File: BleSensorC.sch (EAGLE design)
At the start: 14 parts, among them IC1 SI7020-A10-GM, U1 PIC18(L)F14K22-SOIC

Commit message: Fusion 3D support
Fusion 3D support
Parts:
- removed JP2: (no value), pinhead:PINHD-1X2/90
- removed U$3: SMTU2450N-LF, Battery holders:SMTU2450N-LF
- added B1: SMTU2450N-LF.TR, esao:SMTU2450N-LF.TR
- added C6: 1nF, resistor:C-EUC0805
- added C7: 1uF, resistor:C-EUC0805
- added MK1: SPH0644HM4H-1-3D, esao:SPH0644HM4H-1-3D
- added Q1: SI2333DDS-T1-GE3, esao:SI2333DDS-T1-GE3
- added R4: 4k7, resistor:R-EU_R0805
- added T1: BPW85C-L90, esao:BPW85C-L90
- C5: value 1nF -> 100nF
- IC1: value SI7020-A10-GM -> SI7020-A20-GM; device si70xx-10:SI7020-A10-GM -> esao:SI7020-A20-GM
- JP1: value (none) -> PINHD-1X8; device pinhead:PINHD-1X6 -> esao:PINHD-1X8
- R1, R2, R3: device resistor:R-EU_M0805 -> resistor:R-EU_R0805
- U1: value PIC18(L)F14K22-SOIC -> PIC16LF18446-I_SS; device Microchip PIC18F12K44_esao:PIC18(L)F14K22-SOIC -> SamacSys_Parts:PIC16LF18446-I_SS
- U2: value (none) -> RN4871-I; device Microchip RN4871:RN4871SMD -> esao:RN4871-I
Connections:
- removed net RA3_MCLR_VPP: JP1.1, U1.RA3/MCRL/VPP
- removed net SCL: IC1.SCL, R3.2, U1.RB6
- removed net SDA: IC1.SDA, R2.2, U1.RB4
- removed net U_MON: U1.RA2
- new net !MCLR!_VPP_RA3: JP1.1, U1.!MCLR!/VPP/RA3
- new net +B: B1.+B, Q1.D
- new net SCL1: IC1.SCL, R3.2, U1.RC0
- new net SCL2: MK1.CLOCK, U1.RC6
- new net SDA1: IC1.SDA, R2.2, U1.RC1
- new net SDA2: MK1.DATA, U1.RC7
- net GND: now also B1.-B, C6.2, C7.2, IC1.TGND, MK1.GND_1, MK1.GND_2, Q1.G, U2.GND13; no longer U$3.-B, U2.GND
- net IMP: now also C6.1, T1.E; no longer C5.1, JP2.2
- net PIC_RX: now also U1.RC5; no longer U1.RB5/RX/DT
- net PIC_TX: now also U1.RC4; no longer U1.RB7/TX/CK
- net RA0_ICSPDAT: now also U1.RA0/ICSPDAT; no longer U1.RA0
- net RA1_ICSPCLK: now also U1.RA1/ICSPCLK; no longer U1.RA1
- net RST: now also C7.1, R4.1, U2.RST; no longer U2.RST_N
- net UART_RX_IND: now also U1.RC3; no longer U1.RC0
- net VDD: now also C5.1, MK1.SELECT, MK1.VDD, Q1.S, R4.2, T1.C; no longer JP2.1, U$3.+B
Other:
- note added: "IC1"
- note added: "MK1"
- note removed: "C1"
- moved on the sheet: C3, C4, C5, R1, R2, R3

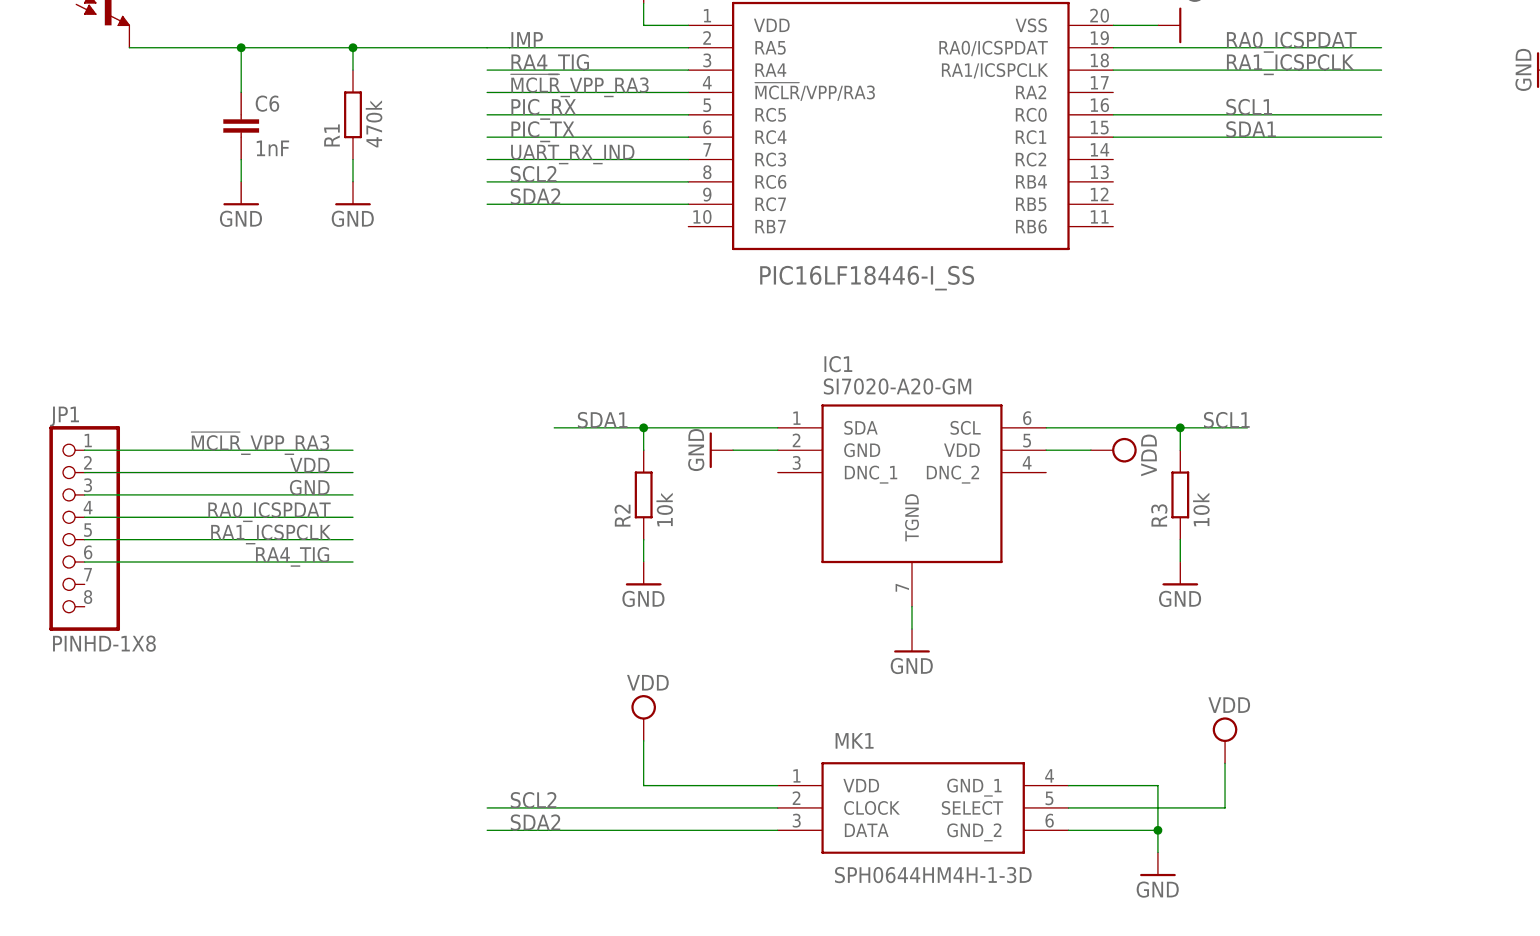
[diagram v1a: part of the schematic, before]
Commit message: JP1 & JP2
JP1 1X6
JP2 2X3
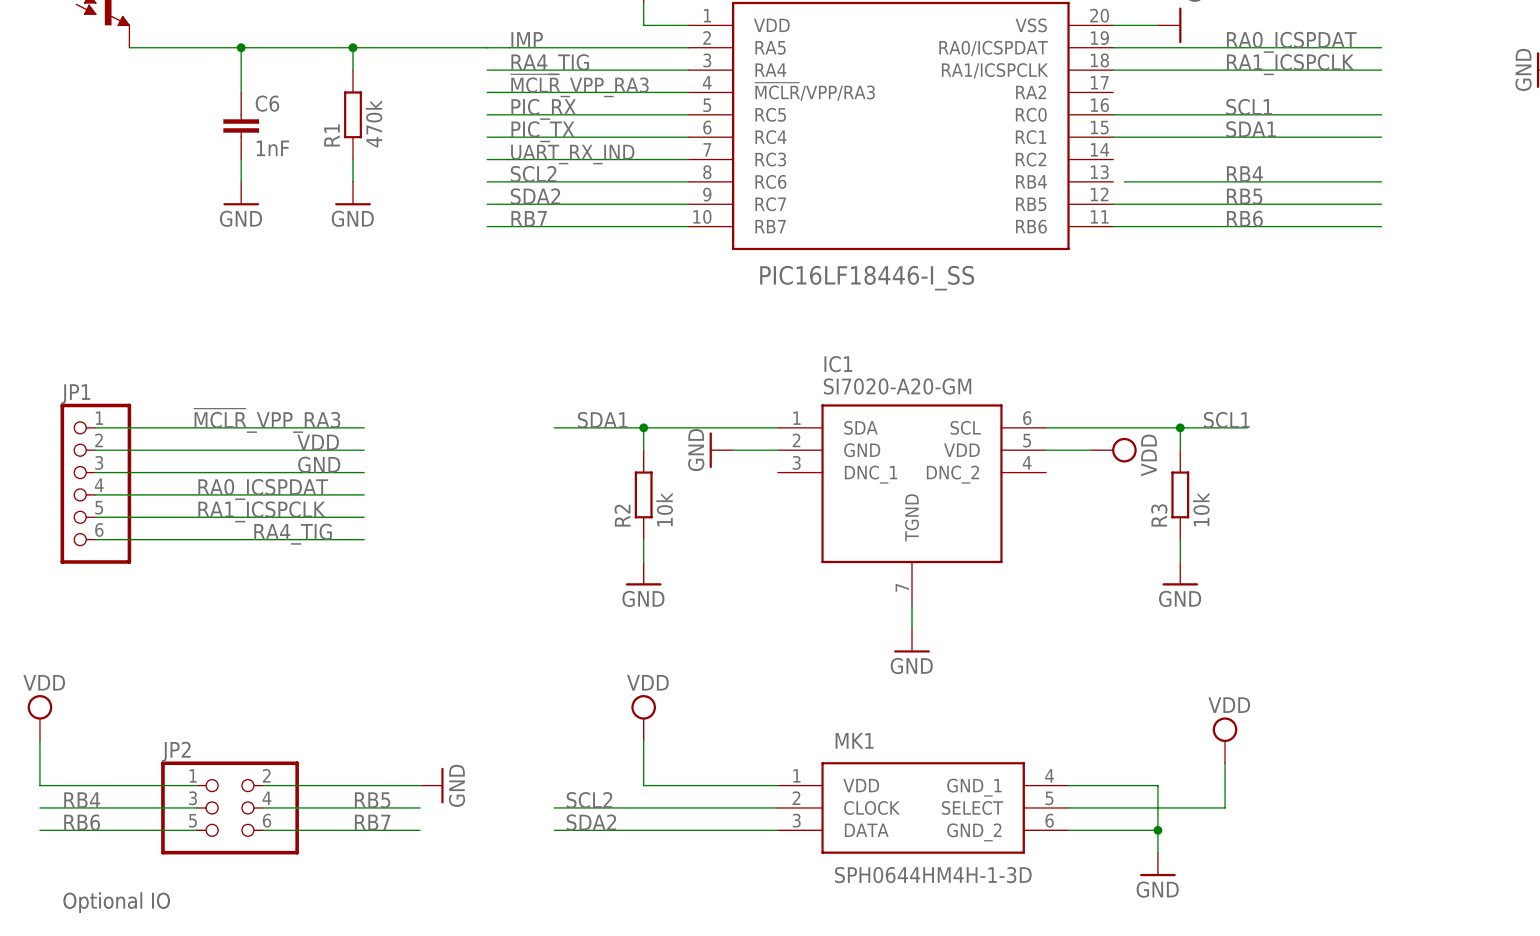
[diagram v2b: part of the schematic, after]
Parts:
- added JP2: (no value), pinhead:PINHD-2X3
- JP1: value PINHD-1X8 -> (none); device esao:PINHD-1X8 -> esao:PINHD-1X6-S
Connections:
- new net RB4: JP2.3
- new net RB5: JP2.4, U1.RB5
- new net RB6: JP2.5, U1.RB6
- new net RB7: JP2.6, U1.RB7
- net GND: now also JP2.2
- net VDD: now also JP2.1
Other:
- note added: "Optional IO"

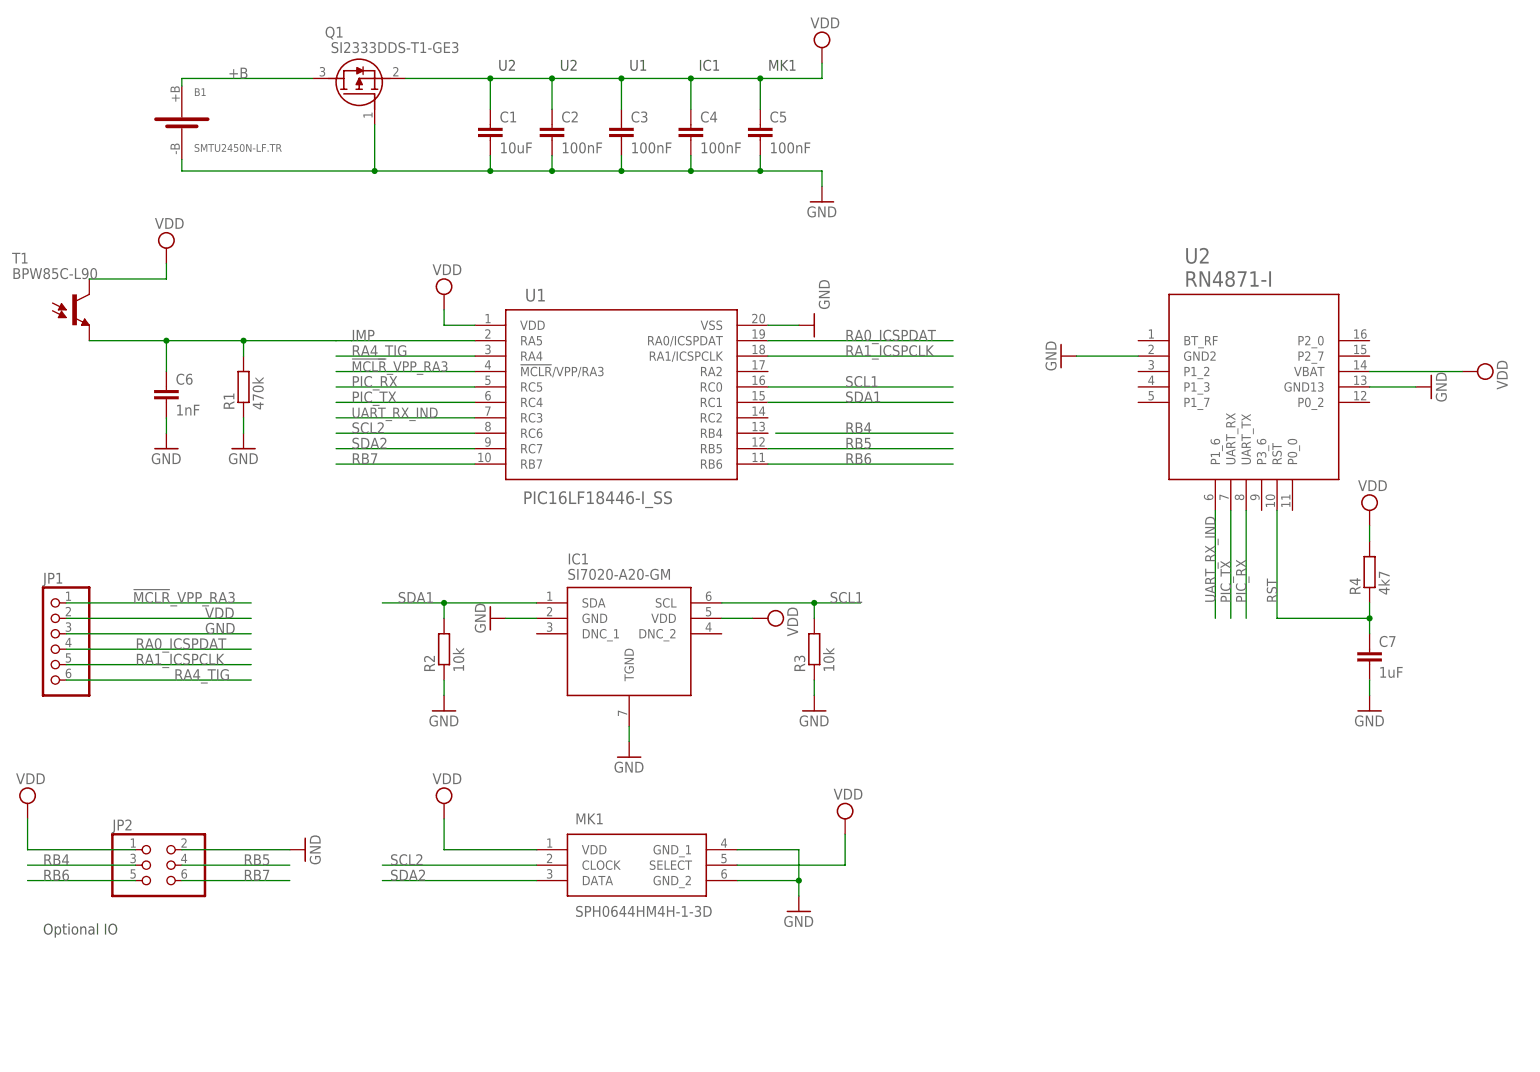
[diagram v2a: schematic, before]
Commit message: T1 phototransistor
Changed T1 to Vishay VEMT2523
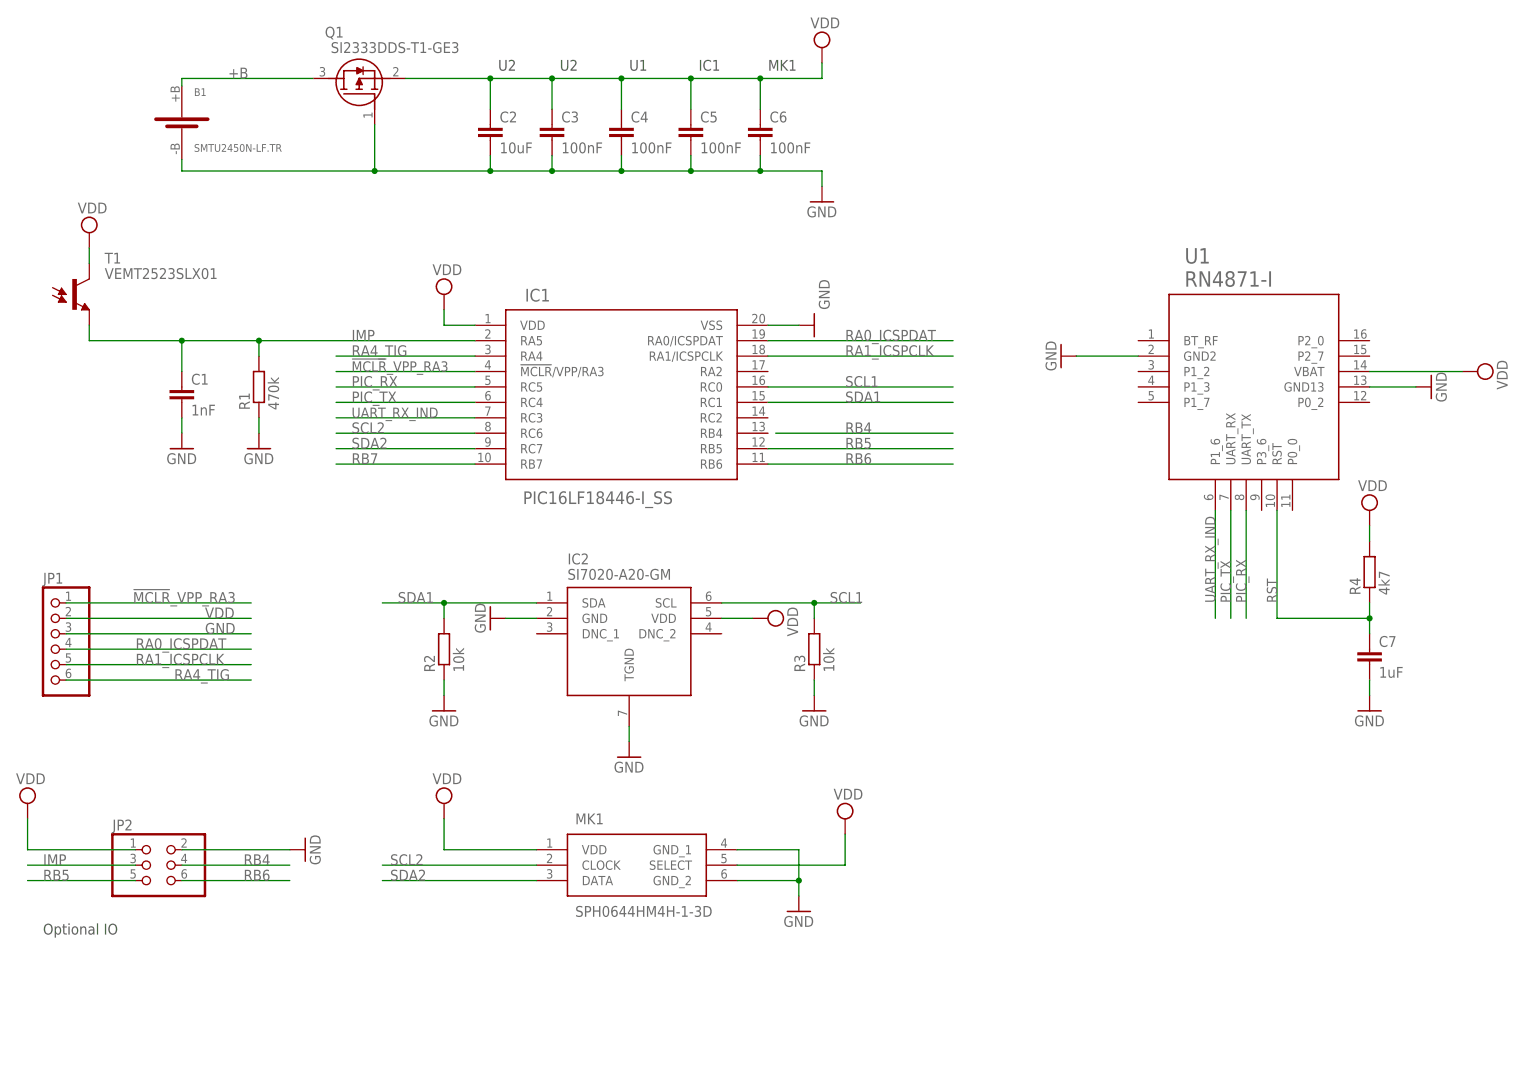
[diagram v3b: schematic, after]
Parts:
- removed U2: RN4871-I, esao:RN4871-I
- added IC2: SI7020-A20-GM, esao:SI7020-A20-GM
- C1: value 10uF -> 1nF; device resistor:C-EUC0805 -> resistor:C-EUC0603
- C2: value 100nF -> 10uF; device resistor:C-EUC0805 -> resistor:C-EUC0603
- C3, C4, C5, C7: device resistor:C-EUC0805 -> resistor:C-EUC0603
- C6: value 1nF -> 100nF; device resistor:C-EUC0805 -> resistor:C-EUC0603
- IC1: value SI7020-A20-GM -> PIC16LF18446-I_SS; device esao:SI7020-A20-GM -> SamacSys_Parts:PIC16LF18446-I_SS
- R1, R2, R3, R4: device resistor:R-EU_R0805 -> resistor:R-EU_R0603
- T1: value BPW85C-L90 -> VEMT2523SLX01; device esao:BPW85C-L90 -> esao:VEMT2523SLX01
- U1: value PIC16LF18446-I_SS -> RN4871-I; device SamacSys_Parts:PIC16LF18446-I_SS -> esao:RN4871-I
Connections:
- net !MCLR!_VPP_RA3: now also IC1.!MCLR!/VPP/RA3; no longer U1.!MCLR!/VPP/RA3
- net GND: now also IC1.VSS, IC2.GND, IC2.TGND, U1.GND13, U1.GND2; no longer IC1.GND, IC1.TGND, U1.VSS, U2.GND13, U2.GND2
- net IMP: now also C1.1, IC1.RA5, JP2.3; no longer C6.1, U1.RA5
- net PIC_RX: now also IC1.RC5, U1.UART_TX; no longer U1.RC5, U2.UART_TX
- net PIC_TX: now also IC1.RC4, U1.UART_RX; no longer U1.RC4, U2.UART_RX
- net RA0_ICSPDAT: now also IC1.RA0/ICSPDAT; no longer U1.RA0/ICSPDAT
- net RA1_ICSPCLK: now also IC1.RA1/ICSPCLK; no longer U1.RA1/ICSPCLK
- net RA4_TIG: now also IC1.RA4; no longer U1.RA4
- net RB4: now also JP2.4; no longer JP2.3
- net RB5: now also IC1.RB5, JP2.5; no longer JP2.4, U1.RB5
- net RB6: now also IC1.RB6, JP2.6; no longer JP2.5, U1.RB6
- net RB7: now also IC1.RB7; no longer JP2.6, U1.RB7
- net RST: now also U1.RST; no longer U2.RST
- net SCL1: now also IC1.RC0, IC2.SCL; no longer IC1.SCL, U1.RC0
- net SCL2: now also IC1.RC6; no longer U1.RC6
- net SDA1: now also IC1.RC1, IC2.SDA; no longer IC1.SDA, U1.RC1
- net SDA2: now also IC1.RC7; no longer U1.RC7
- net UART_RX_IND: now also IC1.RC3, U1.P1_6; no longer U1.RC3, U2.P1_6
- net VDD: now also C6.1, IC2.VDD, U1.VBAT; no longer C1.1, U1.VDD, U2.VBAT
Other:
- moved on the sheet: C1, C2, C3, C4, C5, C6, R1, T1

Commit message: Manual routing
Manual routing
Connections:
- net RB4: now also IC1.RB4
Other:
- note added: "IC2"
- note removed: "U2"
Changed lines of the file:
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@@
 <sheet>
 <plain>
-<text x="87.63" y="168.91" size="1.778" layer="97">U2</text>
-<text x="97.79" y="168.91" size="1.778" layer="97">U2</text>
-<text x="120.65" y="168.91" size="1.778" layer="97">IC1</text>
-<text x="109.22" y="168.91" size="1.778" layer="97">U1</text>
+<text x="87.63" y="168.91" size="1.778" layer="97">U1</text>
+<text x="97.79" y="168.91" size="1.778" layer="97">U1</text>
+<text x="109.22" y="168.91" size="1.778" layer="97">IC1</text>
+<text x="120.65" y="168.91" size="1.778" layer="97">IC2</text>
 <text x="132.08" y="168.91" size="1.778" layer="97">MK1</text>
 <text x="12.7" y="26.67" size="1.778" layer="97">Optional IO</text>
@@
 <net name="RB4" class="0">
 <segment>
-<wire x1="133.35" y1="109.22" x2="162.56" y2="109.22" width="0.1524" layer="91"/>
-<label x="144.78" y="109.22" size="1.778" layer="95"/>
-</segment>
-<segment>
 <pinref part="JP2" gate="A" pin="4"/>
 <wire x1="35.56" y1="38.1" x2="53.34" y2="38.1" width="0.1524" layer="91"/>
 <label x="45.72" y="38.1" size="1.778" layer="95"/>
 </segment>
-</net>
+<segment>
+<pinref part="IC1" gate="G$1" pin="RB4"/>
+<wire x1="132.08" y1="109.22" x2="162.56" y2="109.22" width="0.1524" layer="91"/>
+<label x="144.78" y="109.22" size="1.778" layer="95"/>
+</segment>
+</net>
